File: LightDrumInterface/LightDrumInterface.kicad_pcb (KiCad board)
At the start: 2 copper layers, 108 x 83 mm, 75 parts, among them J1 MIDI-IN, J3 DEBUG-CONN, J4 PWR-CONN, J5 MIDI-OUT, J6 0541323662, Q1 NX6008NBKWX, Q2 NX6008NBKWX, Q3 NX6008NBKWX, Q4 NX6008NBKWX, SW1 RESET-SW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

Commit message: Fix BOM generator options
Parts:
- renumbered REF** to ENCLOSURE1
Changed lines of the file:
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@@
   (footprint "Daxxn_Enclosures:LeMotech_Black_ENC-115x90" locked (layer "F.Cu")
     (at 73.15 66)
-    (attr board_only)
-    (fp_text reference "REF**" (at -57 -46 unlocked) (layer "F.Fab")
+    (attr board_only exclude_from_bom)
+    (fp_text reference "ENCLOSURE1" (at -57 -46 unlocked) (layer "Cmts.User")
         (effects (font (size 1 1) (thickness 0.15)) (justify left))
     )
-    (fp_text value "LeMotech_Black_ENC-115x90" (at -57 -48 unlocked) (layer "F.Fab")
+    (fp_text value "LeMotech_Black_ENC-115x90" (at -57 -48 unlocked) (layer "Cmts.User")
         (effects (font (size 1 1) (thickness 0.15)) (justify left))
     )
-    (fp_text user "${REFERENCE}" (at -57 -50 unlocked) (layer "F.Fab")
+    (fp_text user "https://www.amazon.com/gp/product/B0895J3SWL/ref=ox_sc_act_title_3?smid=A1NFM2368P534K&th=1" (at -57.15 -50) (layer "Cmts.User")
         (effects (font (size 1 1) (thickness 0.15)) (justify left))
     )
-    (fp_text user "https://www.amazon.com/gp/product/B0895J3SWL/ref=ox_sc_act_title_3?smid=A1NFM2368P534K&th=1" (at -57.15 -50) (layer "User.9")
+    (fp_text user "${REFERENCE}" (at -57 -50 unlocked) (layer "Cmts.User") hide
         (effects (font (size 1 1) (thickness 0.15)) (justify left))
     )

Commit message: PCB Lock REV11
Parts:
- removed D-MD1, D-ML1, D-MR1, D-MU1: RED, LED_SMD:LED_0805_2012Metric
- added C10: 4.7uF, Capacitor_SMD:C_0805_2012Metric, F.Cu at (124.2, 56.9)
- added C11: 100nF, Capacitor_SMD:C_0402_1005Metric, F.Cu at (124.2, 55.4)
- added D2: APHBM2012QBDSURKC, Daxxn_LEDs:APHBM-2012, F.Cu at (83.2, 106.4)
- added D3: APHBM2012QBDSURKC, Daxxn_LEDs:APHBM-2012, F.Cu at (102.2, 106.4)
- added H1: M2.5, MountingHole:MountingHole_2.7mm_M2.5_Pad_Via, F.Cu at (33.6, 101.0)
- added H2: M2.5, MountingHole:MountingHole_2.7mm_M2.5_Pad_Via, F.Cu at (112.7, 101.0)
- added H3: M2.5, MountingHole:MountingHole_2.7mm_M2.5_Pad_Via, F.Cu at (112.7, 31.0)
- added H4: M2.5, MountingHole:MountingHole_2.7mm_M2.5_Pad_Via, F.Cu at (33.6, 31.0)
- added R25: 47K, Resistor_SMD:R_0402_1005Metric, F.Cu at (118.0, 58.6)
- added R26: 47K, Resistor_SMD:R_0402_1005Metric, F.Cu at (118.0, 57.5)
- added R27: 47K, Resistor_SMD:R_0402_1005Metric, F.Cu at (118.0, 56.5)
- added R28: 47K, Resistor_SMD:R_0402_1005Metric, F.Cu at (118.0, 52.0)
- added R29: 47K, Resistor_SMD:R_0402_1005Metric, F.Cu at (118.0, 51.0)
- C1, C2, C4, C9: footprint Capacitor_SMD:C_0603_1608Metric -> Capacitor_SMD:C_0402_1005Metric
- C5, C6, C7, C8: footprint Capacitor_SMD:C_0805_2012Metric -> Capacitor_SMD:C_0402_1005Metric
- D-STA1: value ORANGE -> AMBER
- D-VCC1, D-VDD1, D-VDRIVE1: value YELLOW -> BLUE
- D1: value IN4848 -> 1N4148
- J3: value DEBUG-CONN -> Micro_SD_Card; footprint Connector_JST:JST_XH_B4B-XH-A_1x04_P2.50mm_Vertical -> Daxxn_Connectors:MEM2061-01-188-00-A
- R1, R13, R14, R15, R3, R4, R5, R6, R7, R8: footprint Resistor_SMD:R_0805_2012Metric -> Resistor_SMD:R_0402_1005Metric
- R10, R11, R12, R9: value 100 -> 300; footprint Resistor_SMD:R_0805_2012Metric -> Resistor_SMD:R_0402_1005Metric
- R16: value 560Ω -> 560; footprint Resistor_SMD:R_0805_2012Metric -> Resistor_SMD:R_0402_1005Metric
- R17, R18, R20, R21, R22: value 10KΩ -> 10K; footprint Resistor_SMD:R_0805_2012Metric -> Resistor_SMD:R_0402_1005Metric
- R19, R23, R24: value 220Ω -> 220; footprint Resistor_SMD:R_0805_2012Metric -> Resistor_SMD:R_0402_1005Metric
- R2: value 550 -> 560; footprint Resistor_SMD:R_0805_2012Metric -> Resistor_SMD:R_0402_1005Metric
- U3: value PC817 -> APC-817A1-SL; footprint Package_DIP:DIP-4_W7.62mm -> Package_DIP:SMDIP-4_W7.62mm
- U4: value 74AUP2G04 -> SN74AUP2G04
- moved J3 87.5 mm to (118.2, 56.7), turned to -90 degrees
- moved J4 44.7 mm to (86.9, 82.2), turned to 180 degrees
- moved J6 30.3 mm to (61.1, 71.1), turned to 180 degrees
- moved R23 18.1 mm to (100.5, 70.3)
- moved C9 15.1 mm to (98.0, 64.1), turned to 90 degrees
- moved J5 14.3 mm to (103.2, 70.8)
- moved R24 14.3 mm to (99.5, 65.7)
- moved U4 14.3 mm to (95.8, 65.0)
- moved R10 12.8 mm to (58.2, 87.0)
- moved R11 12.8 mm to (54.2, 87.0)
- moved R12 12.8 mm to (52.2, 87.0)
- moved R9 12.8 mm to (56.2, 87.0)
- moved R20 3.12 mm to (95.3, 84.1)
- moved D-BK1 3.00 mm to (64.7, 91.4), turned to -45 degrees
- moved D-BK2 3.00 mm to (64.7, 105.4), turned to 45 degrees
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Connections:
- DA1 pad 11: Net-(DA1-Pad11) -> Net-(U1-~{OUT9})
- DA1 pad 12: Net-(DA1-Pad12) -> Net-(U1-~{OUT8})
- J3 pad 1: VCC -> Net-(J3-DAT2)
- J3 pad 2: /I2C-SCLK -> /SD-CD
- J3 pad 3: /I2C-SDA -> /SD-CMD
- J3 pad 4: GND -> VDD
- J6 pad 11: /ENC2-A -> VCC
- J6 pad 13: VCC -> /I2C-SDA
- J6 pad 14: /I2C-SDA -> /ENC2-A
- J6 pad 15: /ENC2-SW -> /I2C-SCLK
- J6 pad 16: /SCR-TX -> /ENC1-A
- J6 pad 17: /I2C-SCLK -> /SD-CD
- J6 pad 18: /SCR-RX -> /ENC2-SW
- J6 pad 23: /GRAPH-LE -> /ENC1-B
- J6 pad 24: /MENU-LEFT -> /GRAPH-SDI
- J6 pad 25: /GRAPH-~{OE} -> /GRAPH-LE
- J6 pad 27: /ENC1-B -> /GRAPH-~{OE}
- J6 pad 28: GND -> /SD-CLK
- J6 pad 29: GND -> /SD-D0
- J6 pad 3: GND -> /MIDI-IN
- J6 pad 30: /STRIP-PWR -> /SD-CMD
- J6 pad 31: /DIAG-STATUS -> /STRIP-PWR
- J6 pad 32: /DIAG-DEBUG -> /DIAG-STATUS
- J6 pad 33: /AUDIO-SRC-IND -> /DIAG-DEBUG
- J6 pad 34: GND -> /AUDIO-SRC-IND
- J6 pad 5: /MIDI-IN -> GND
- J6 pad 6: /GRAPH-SDI -> /GRAPH-CLK
- J6 pad 7: GND -> /SCR-TX
- J6 pad 8: /GRAPH-CLK -> /MENU-LEFT
- J6 pad 9: /ENC1-A -> /SCR-RX
- U1 pad 13: Net-(DA1-Pad11) -> Net-(U1-~{OUT8})
- U1 pad 14: Net-(DA1-Pad12) -> Net-(U1-~{OUT9})
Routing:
- net /SD-D0: track 0.00 -> 86.5 mm, vias 0 -> 3
- net /SD-CMD: track 0.00 -> 83.9 mm, vias 0 -> 3
- net /SD-CLK: track 0.00 -> 80.4 mm, vias 0 -> 4
- net /SD-CD: track 0.00 -> 79.1 mm, vias 0 -> 1
- net VCC: track 428.0 -> 359.1 mm, vias 16 -> 14
- net /I2C-SDA: track 71.0 -> 9.83 mm
- net /I2C-SCLK: track 67.6 -> 7.34 mm, vias 2 -> 1
- net Vdrive: track 152.8 -> 99.8 mm, vias 1 -> 3
- net /MIDI-OUT: track 81.4 -> 31.0 mm, vias 3 -> 1
- net /~{RESET}: track 26.5 -> 72.2 mm
- net Net-(D3B-R-K): track 53.6 -> 97.7 mm
- net /DIAG-DEBUG: track 73.4 -> 34.9 mm, vias 1 -> 3
- net Net-(D3A-B-K): track 68.8 -> 105.8 mm, vias 6 -> 4
- net /AUDIO-SRC-IND: track 92.3 -> 56.3 mm, vias 3 -> 5
- net /DIAG-STATUS: track 70.0 -> 34.3 mm, vias 1 -> 3
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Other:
- board text added: "+"
- board text added: "-"
- board text added: "REV11"
- board text removed: "CLOCK"
- board text removed: "DATA"
- board text removed: "GND"
- board text removed: "REV10"

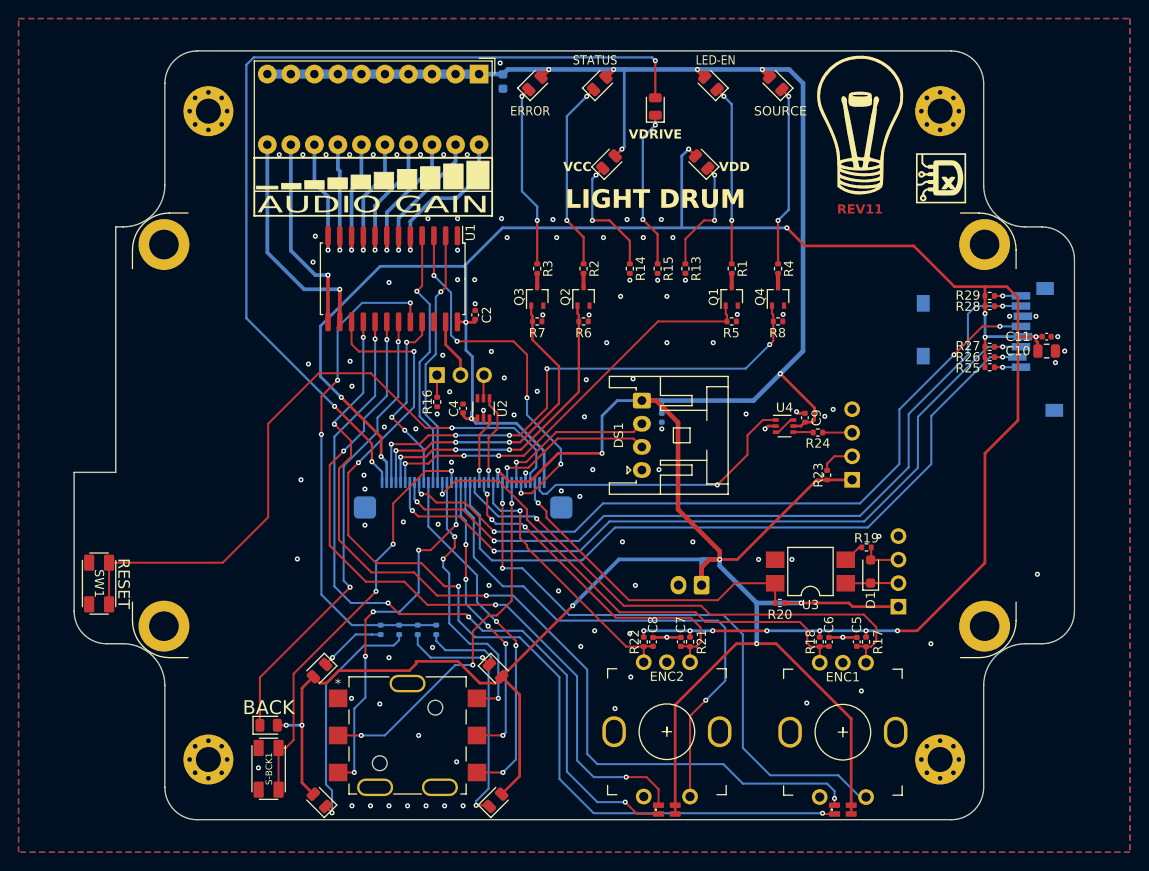
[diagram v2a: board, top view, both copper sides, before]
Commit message: Fix backwards Connector - Initial Testing
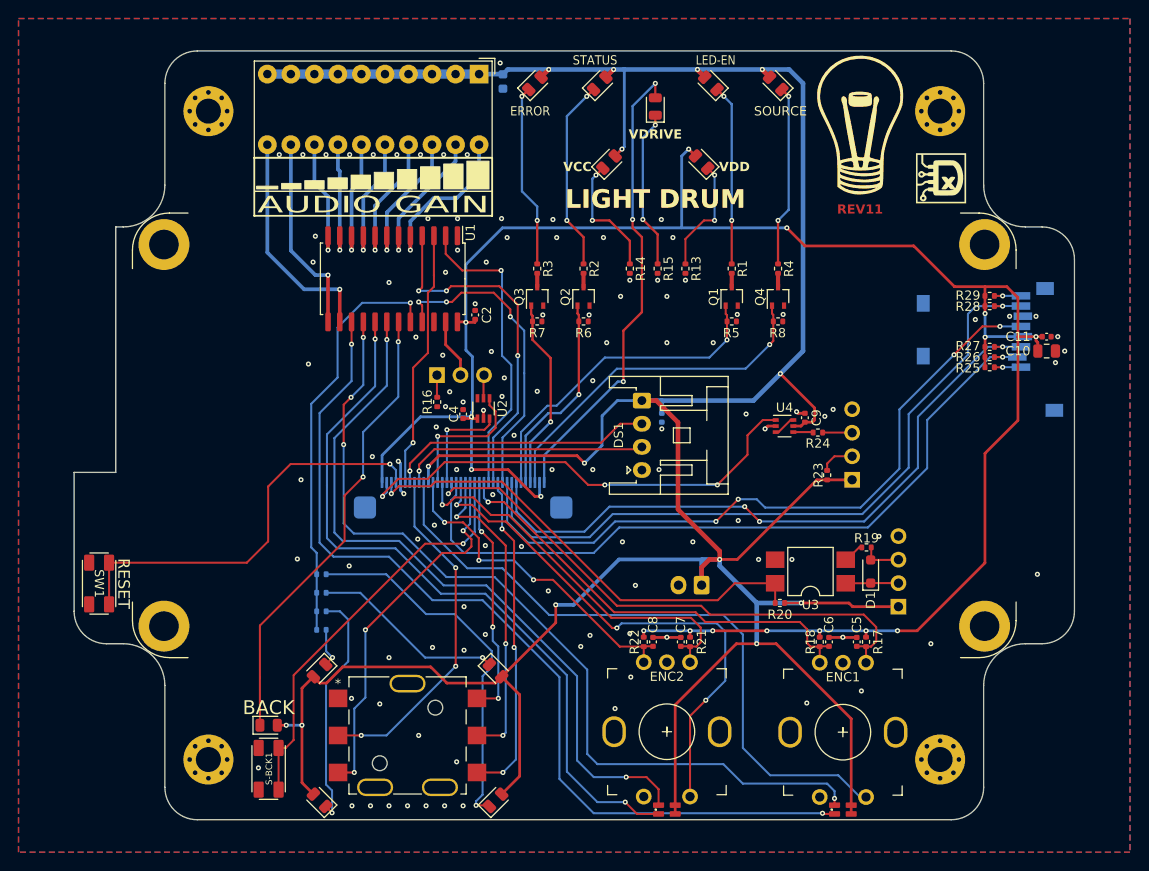
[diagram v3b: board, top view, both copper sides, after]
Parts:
- SN1: value JS5208 -> SW6_JS5208_ESW
- moved R10 13.8 mm to (45.9, 81.0), turned to 180 degrees
- moved R9 11.1 mm to (45.9, 83.0), turned to 180 degrees
- moved R11 8.63 mm to (45.9, 85.0), turned to 180 degrees
- moved R12 6.40 mm to (45.9, 87.0), turned to 180 degrees
- moved C4 0.60 mm to (61.1, 63.7)
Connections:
- J6 pad 1: VDD -> Vdrive
- J6 pad 10: /ENC1-SW -> /GRAPH-~{OE}
- J6 pad 11: VCC -> /MENU-DOWN
- J6 pad 12: /ENC2-B -> /GRAPH-LE
- J6 pad 13: /I2C-SDA -> /GRAPH-SDI
- J6 pad 14: /ENC2-A -> /ENC1-B
- J6 pad 15: /I2C-SCLK -> /MENU-UP
- J6 pad 16: /ENC1-A -> /MENU-BACK
- J6 pad 17: /SD-CD -> /MENU-ACT
- J6 pad 18: /ENC2-SW -> /MENU-RIGHT
- J6 pad 19: /MENU-RIGHT -> /ENC2-SW
- J6 pad 2: /MIDI-OUT -> VDD
- J6 pad 20: /MENU-ACT -> /SD-CD
- J6 pad 21: /MENU-BACK -> /ENC1-A
- J6 pad 22: /MENU-UP -> /I2C-SCLK
- J6 pad 23: /ENC1-B -> /ENC2-A
- J6 pad 24: /GRAPH-SDI -> /I2C-SDA
- J6 pad 25: /GRAPH-LE -> /ENC2-B
- J6 pad 26: /MENU-DOWN -> VCC
- J6 pad 27: /GRAPH-~{OE} -> /ENC1-SW
- J6 pad 28: /SD-CLK -> /SCR-RX
- J6 pad 29: /SD-D0 -> /MENU-LEFT
- J6 pad 3: /MIDI-IN -> /AUDIO-SRC-IND
- J6 pad 30: /SD-CMD -> /SCR-TX
- J6 pad 31: /STRIP-PWR -> /GRAPH-CLK
- J6 pad 32: /DIAG-STATUS -> GND
- J6 pad 33: /DIAG-DEBUG -> /~{RESET}
- J6 pad 34: /AUDIO-SRC-IND -> /MIDI-IN
- J6 pad 35: VDD -> /MIDI-OUT
- J6 pad 36: Vdrive -> VDD
- J6 pad 4: /~{RESET} -> /DIAG-DEBUG
- J6 pad 5: GND -> /DIAG-STATUS
- J6 pad 6: /GRAPH-CLK -> /STRIP-PWR
- J6 pad 7: /SCR-TX -> /SD-CMD
- J6 pad 8: /MENU-LEFT -> /SD-D0
- J6 pad 9: /SCR-RX -> /SD-CLK
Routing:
- net Vdrive: track 99.8 -> 50.8 mm
- net /~{RESET}: track 72.2 -> 45.0 mm
- net VDD: track 237.0 -> 216.2 mm
- net /MIDI-OUT: track 31.0 -> 50.9 mm, vias 1 -> 3
- net /AUDIO-SRC-IND: track 56.3 -> 37.9 mm, vias 5 -> 1
- net /MIDI-IN: track 35.6 -> 51.4 mm
- net Net-(D-BK2-K): track 25.5 -> 40.2 mm
- net /DIAG-DEBUG: track 34.9 -> 20.9 mm, vias 3 -> 1
- net /GRAPH-~{OE}: track 20.7 -> 33.6 mm
- net /GRAPH-CLK: track 40.7 -> 27.9 mm, vias 5 -> 1
- net /DIAG-STATUS: track 34.3 -> 22.3 mm, vias 3 -> 1
- net /SD-CMD: track 83.9 -> 72.2 mm
- net /SCR-TX: track 17.5 -> 28.9 mm
- net Net-(D-BK1-K): track 9.71 -> 20.8 mm
- net /SD-D0: track 86.5 -> 76.8 mm, vias 3 -> 1
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
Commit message: Organize old files and generate interface gerbers
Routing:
- net GND: vias 115 -> 123
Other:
- board text added: "REV12"
- board text added: "STRIP"
- board text removed: "LED-EN"
- board text removed: "REV11"

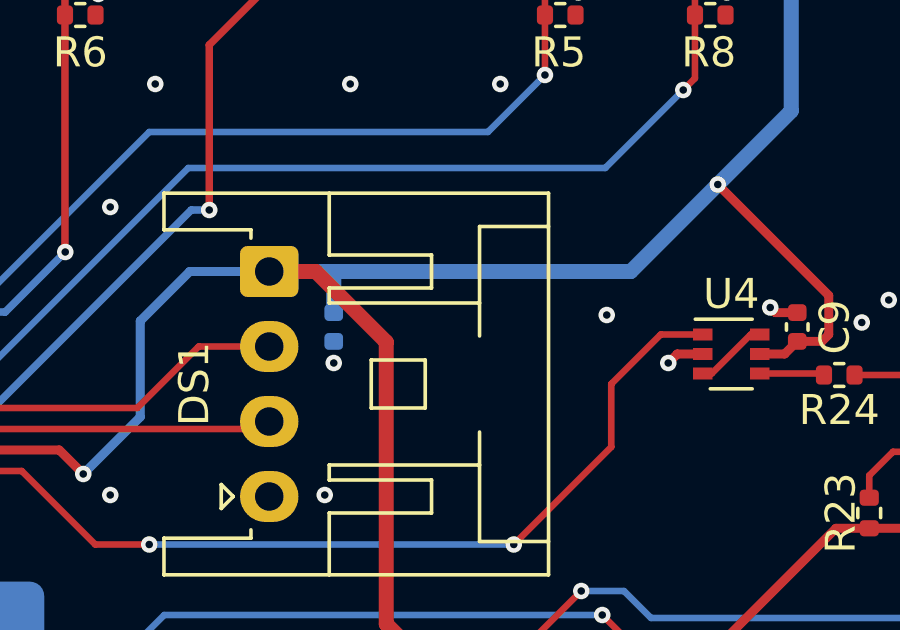
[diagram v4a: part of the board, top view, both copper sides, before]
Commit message: add screen control and more display layout
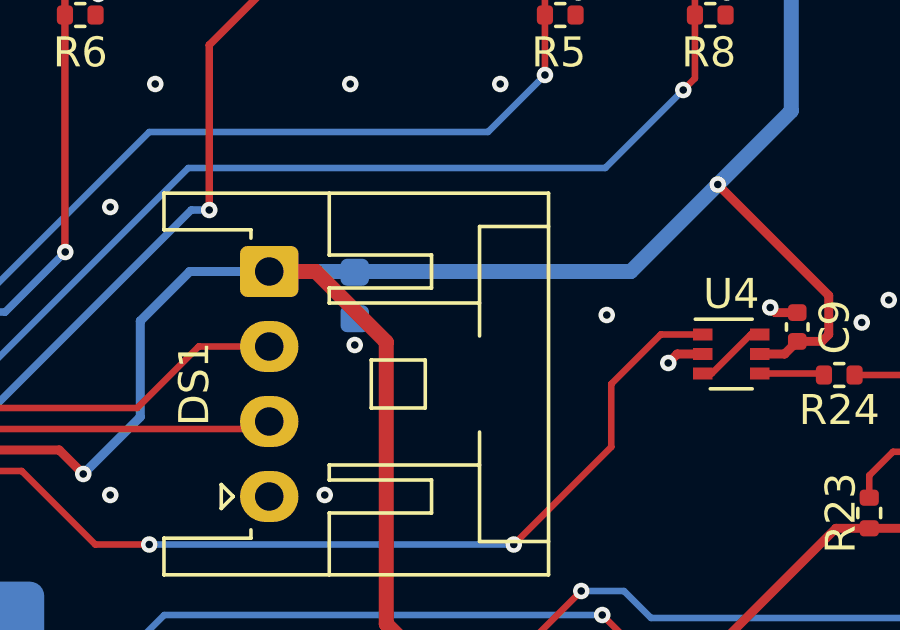
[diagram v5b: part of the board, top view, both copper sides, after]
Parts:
- C1: value 100nF -> 1uF; footprint Capacitor_SMD:C_0402_1005Metric -> Capacitor_SMD:C_0603_1608Metric
- D1: value 1N4148 -> 1N4448
- SN1: value SW6_JS5208_ESW -> JS5208
- U4: value SN74AUP2G04 -> 74LVC2G14GW
- moved C1 1.26 mm to (83.3, 63.0)
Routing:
- net VCC: track 366.6 -> 365.5 mm
